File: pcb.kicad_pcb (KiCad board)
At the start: 2 copper layers, 0 parts

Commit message: started layout
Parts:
- added C1: 10uF, Capacitor_SMD:C_0805_2012Metric_Pad1.15x1.40mm_HandSolder, F.Cu at (195.3, 56.5)
- added C2: 10uF, Capacitor_SMD:C_0805_2012Metric_Pad1.15x1.40mm_HandSolder, F.Cu at (195.5, 64.0)
- added C3: 4.7uF, Capacitor_SMD:C_0603_1608Metric_Pad1.05x0.95mm_HandSolder, F.Cu at (195.4, 77.2)
- added C4: 100nF, Capacitor_SMD:C_0603_1608Metric_Pad1.05x0.95mm_HandSolder, F.Cu at (195.6, 82.1)
- added C5: 100nF, Capacitor_SMD:C_0603_1608Metric_Pad1.05x0.95mm_HandSolder, F.Cu at (195.5, 72.7)
- added C6: 100nF, Capacitor_SMD:C_0603_1608Metric_Pad1.05x0.95mm_HandSolder, F.Cu at (195.7, 92.0)
- added C7: 100nF, Capacitor_SMD:C_0603_1608Metric_Pad1.05x0.95mm_HandSolder, F.Cu at (195.6, 87.0)
- added C8: 100nF, Capacitor_SMD:C_0603_1608Metric_Pad1.05x0.95mm_HandSolder, F.Cu at (195.5, 68.3)
- added G1: GPS_NEO_6M_module, components_ece445:GPS_NEO_6M_module, F.Cu at (153.3, 70.9)
- added J1: Conn_01x02, Connector_PinHeader_2.54mm:PinHeader_1x02_P2.54mm_Vertical, F.Cu at (172.8, 32.2)
- added J2: Conn_01x03, Connector_PinHeader_2.54mm:PinHeader_1x03_P2.54mm_Vertical, F.Cu at (112.3, 35.5)
- added J3: Conn_01x03, Connector_PinHeader_2.54mm:PinHeader_1x03_P2.54mm_Vertical, F.Cu at (112.6, 51.8)
- added J4: Conn_01x02, Connector_PinHeader_2.54mm:PinHeader_1x02_P2.54mm_Vertical, F.Cu at (108.8, 96.2)
- added J5: Conn_01x02, Connector_PinHeader_2.54mm:PinHeader_1x02_P2.54mm_Vertical, F.Cu at (120.2, 96.2)
- added J6: Conn_02x05_Odd_Even, Connector_PinHeader_2.54mm:PinHeader_2x05_P2.54mm_Vertical, F.Cu at (93.3, 76.2)
- added Q1: 2N3904, Package_TO_SOT_THT:TO-92_Inline, F.Cu at (99.6, 33.9)
- added Q2: 2N3904, Package_TO_SOT_THT:TO-92_Inline, F.Cu at (99.5, 51.4)
- added Q3: 2N3904, Package_TO_SOT_THT:TO-92_Inline, F.Cu at (99.5, 42.6)
- added Q4: 2N3904, Package_TO_SOT_THT:TO-92_Inline, F.Cu at (99.5, 61.3)
- added R1: 4.7K, Resistor_SMD:R_1206_3216Metric_Pad1.42x1.75mm_HandSolder, F.Cu at (89.0, 36.0)
- added R2: 4.7K, Resistor_SMD:R_1206_3216Metric_Pad1.42x1.75mm_HandSolder, F.Cu at (89.2, 41.1)
- added R3: 1K, Resistor_SMD:R_1206_3216Metric_Pad1.42x1.75mm_HandSolder, F.Cu at (89.1, 46.2)
- added R4: 4.7K, Resistor_SMD:R_1206_3216Metric_Pad1.42x1.75mm_HandSolder, F.Cu at (89.1, 51.2)
- added R5: 4.7K, Resistor_SMD:R_1206_3216Metric_Pad1.42x1.75mm_HandSolder, F.Cu at (89.1, 56.5)
- added R6: 1K, Resistor_SMD:R_1206_3216Metric_Pad1.42x1.75mm_HandSolder, F.Cu at (89.1, 61.7)
- added U1: STM32F103C8T6, STM32F103C8T6:QFP50P900X900X160-48N, F.Cu at (121.0, 81.8)
- added U2: Shaft_encoder, components_ece445:shaft_encoder, F.Cu at (158.7, 36.0)
- added U3: compass_accelerometer, components_ece445:compass_accelerometer, F.Cu at (129.7, 60.1)
- added U4: LM1117-3.3, LM1117DT-3_1:TO228P970X238-3N, F.Cu at (195.2, 43.5)
- added U5: 3v7_to_5V_boost, components_ece445:3v7_to_5V_boost, F.Cu at (175.6, 46.5)

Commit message: evan recommmendations
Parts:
- 3V3 LinReg: renamed from U4
- 5V Boost: renamed from U5
- ARM Conn: renamed from J6
- LI-PO BAT: renamed from J1
- Shaft Encoder: renamed from U2
- moved G1 85.2 mm to (91.4, 129.5)
- moved LI-PO BAT 32.3 mm to (160.8, 62.2)
- moved 3V3 LinReg 31.4 mm to (179.2, 70.5)
- moved C2 31.4 mm to (179.5, 91.0)
- moved C3 31.4 mm to (179.4, 104.2)
- moved C4 31.4 mm to (179.6, 109.1)
- moved C5 31.4 mm to (179.5, 99.7)
- moved C6 31.4 mm to (179.7, 119.0)
- moved C7 31.4 mm to (179.6, 114.0)
- moved C8 31.4 mm to (179.5, 95.3)
- moved C1 31.4 mm to (179.3, 83.5)
- moved R4 31.3 mm to (93.0, 82.3), turned to 180 degrees
- moved Shaft Encoder 31.1 mm to (147.5, 65.0)
- moved J3 31.0 mm to (111.6, 82.8)
- moved Q3 31.0 mm to (98.5, 73.7)
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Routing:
- net +3V3: track 0.00 -> 254.1 mm, vias 0 -> 7
- net +5V: track 0.00 -> 202.1 mm
- net PB14: track 0.00 -> 158.4 mm, vias 0 -> 2
- net PB13: track 0.00 -> 67.2 mm, vias 0 -> 2
- net PB3: track 0.00 -> 60.4 mm
- net GND: track 0.00 -> 56.7 mm, vias 0 -> 56
- net PA13: track 0.00 -> 41.1 mm, vias 0 -> 2
- net PA10: track 0.00 -> 36.8 mm
- net PA9: track 0.00 -> 32.7 mm
- net PA14: track 0.00 -> 30.7 mm, vias 0 -> 2
- net Net-(J2-Pad2): track 0.00 -> 28.6 mm
- net Net-(Q1-Pad3): track 0.00 -> 24.2 mm
- net NRST: track 0.00 -> 22.7 mm
- net PB7: track 0.00 -> 20.3 mm, vias 0 -> 2
- net Net-(Q1-Pad2): track 0.00 -> 20.3 mm
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- added copper zone on F.Cu, net +3V3
- added copper zone on B.Cu, net GND
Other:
- board text added: "+"
- board text added: "-"
- board text added: "3V3"
- board text added: "3V7"
- board text added: "5V"
- board text added: "GND"
- board text added: "RX"
- board text added: "TEAM 2 PCB V1.0 3/2/2022"
- board text added: "TX"

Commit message: made changes into pcb, added python code
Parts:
- removed 3V3 LinReg: LM1117-3.3, LM1117DT-3_1:TO228P970X238-3N
- removed 5V Boost: 3v7_to_5V_boost, components_ece445:3v7_to_5V_boost
- removed ARM Conn: Conn_02x05_Odd_Even, Connector_PinHeader_2.54mm:PinHeader_2x05_P2.54mm_Vertical
- removed J5: Conn_01x02, Connector_PinHeader_2.54mm:PinHeader_1x02_P2.54mm_Vertical
- removed LI-PO BAT: Conn_01x02, Connector_PinHeader_2.54mm:PinHeader_1x02_P2.54mm_Vertical
- removed Shaft Encoder: Shaft_encoder, components_ece445:shaft_encoder
- added C9: 100nF, Capacitor_SMD:C_0603_1608Metric_Pad1.05x0.95mm_HandSolder, F.Cu at (123.4, 128.8)
- added J1: Conn_01x02, Connector_PinHeader_2.54mm:PinHeader_1x02_P2.54mm_Vertical, F.Cu at (89.4, 94.5)
- added J10: Conn_01x03-Connector_Generic, Connector_PinSocket_2.54mm:PinSocket_1x03_P2.54mm_Vertical, F.Cu at (115.8, 120.1)
- added J11: Conn_01x03-Connector_Generic, Connector_PinSocket_2.54mm:PinSocket_1x03_P2.54mm_Vertical, F.Cu at (123.2, 112.0)
- added J6: Conn_01x03-Connector_Generic, Connector_PinSocket_2.54mm:PinSocket_1x03_P2.54mm_Vertical, F.Cu at (79.0, 117.9)
- added J7: Conn_01x03-Connector_Generic, Connector_PinSocket_2.54mm:PinSocket_1x03_P2.54mm_Vertical, F.Cu at (119.6, 93.7)
- added J8: Conn_01x03-Connector_Generic, Connector_PinSocket_2.54mm:PinSocket_1x03_P2.54mm_Vertical, F.Cu at (119.6, 102.9)
- added J9: Conn_01x03-Connector_Generic, Connector_PinSocket_2.54mm:PinSocket_1x03_P2.54mm_Vertical, F.Cu at (115.8, 111.3)
- added R7: 10K, Resistor_SMD:R_1206_3216Metric_Pad1.42x1.75mm_HandSolder, F.Cu at (118.6, 128.8)
- added SW1: SW_Push, Button_Switch_SMD:SW_SPST_PTS645, F.Cu at (120.9, 134.6)
- added U2: Shaft_encoder, components_ece445:shaft_encoder, F.Cu at (99.3, 127.3)
- added U4: LM1117-3.3, LM1117DT-3_1:TO228P970X238-3N, F.Cu at (109.2, 102.8)
- added U5: 3v7_to_5V_boost, components_ece445:3v7_to_5V_boost, F.Cu at (106.2, 91.4)
- J4: value Conn_01x02 -> Conn_01x06; footprint Connector_PinHeader_2.54mm:PinHeader_1x02_P2.54mm_Vertical -> Connector_PinHeader_1.27mm:PinHeader_1x06_P1.27mm_Vertical
- moved C8 79.4 mm to (105.7, 124.5), turned to 0 degrees
- moved C5 76.4 mm to (105.7, 119.1), turned to 0 degrees
- moved C1 75.6 mm to (109.2, 111.8)
- moved C3 74.7 mm to (105.7, 115.6), turned to 0 degrees
- moved C7 74.4 mm to (105.7, 122.7), turned to 0 degrees
- moved C4 74.4 mm to (105.7, 117.3), turned to 0 degrees
- moved C6 74.0 mm to (105.7, 120.9), turned to 0 degrees
- moved C2 72.5 mm to (107.2, 95.5)
- moved U3 48.3 mm to (103.1, 132.1), turned to 0 degrees
- moved J2 45.0 mm to (79.0, 97.8)
- moved J3 40.4 mm to (79.0, 106.7)
- moved Q1 32.7 mm to (97.5, 97.5)
- moved R1 32.2 mm to (90.4, 99.1), turned to 180 degrees
- moved U1 31.7 mm to (89.2, 120.1)
- moved R2 29.6 mm to (90.4, 101.6), turned to 180 degrees
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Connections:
- J4 pad 1: PA0 -> +5V
- J4 pad 2: GND -> RX
- U1 pad 12: Net-(U1-Pad12) -> PA2
- U1 pad 13: Net-(U1-Pad13) -> PA3
- U1 pad 16: Net-(U1-Pad16) -> PA6
- U1 pad 21: Net-(U1-Pad21) -> RX
- U1 pad 22: Net-(U1-Pad22) -> TX
- U1 pad 39: PB3 -> Net-(U1-Pad39)
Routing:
- net +3V3: track 254.1 -> 69.9 mm, vias 7 -> 3
- net PB14: track 158.4 -> 0.00 mm, vias 2 -> 0
- net PB13: track 67.2 -> 0.00 mm, vias 2 -> 0
- net PB3: track 60.4 -> 0.00 mm
- net +5V: track 202.1 -> 154.6 mm
- net GND: track 56.7 -> 15.6 mm, vias 56 -> 3
- net PA10: track 36.8 -> 0.00 mm
- net PA9: track 32.7 -> 0.00 mm
- net Net-(J3-Pad2): track 0.00 -> 27.6 mm
- net PA13: track 41.1 -> 14.6 mm
- net PB7: track 20.3 -> 0.00 mm, vias 2 -> 0
- net Net-(Q2-Pad3): track 0.00 -> 18.7 mm, vias 0 -> 2
- net PB6: track 18.2 -> 0.00 mm
- net PA0: track 18.0 -> 0.00 mm
- net PA1: track 17.3 -> 0.00 mm
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- added copper zone on B.Cu, net +3V3
- added copper zone on F.Cu, net GND
- removed copper zone on F.Cu, net +3V3
- removed copper zone on B.Cu, net GND
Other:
- board text removed: "+"
- board text removed: "-"
- board text removed: "3V3"
- board text removed: "3V7"
- board text removed: "5V"
- board text removed: "GND"
- board text removed: "RX"
- board text removed: "TEAM 2 PCB V1.0 3/2/2022"
- board text removed: "TX"

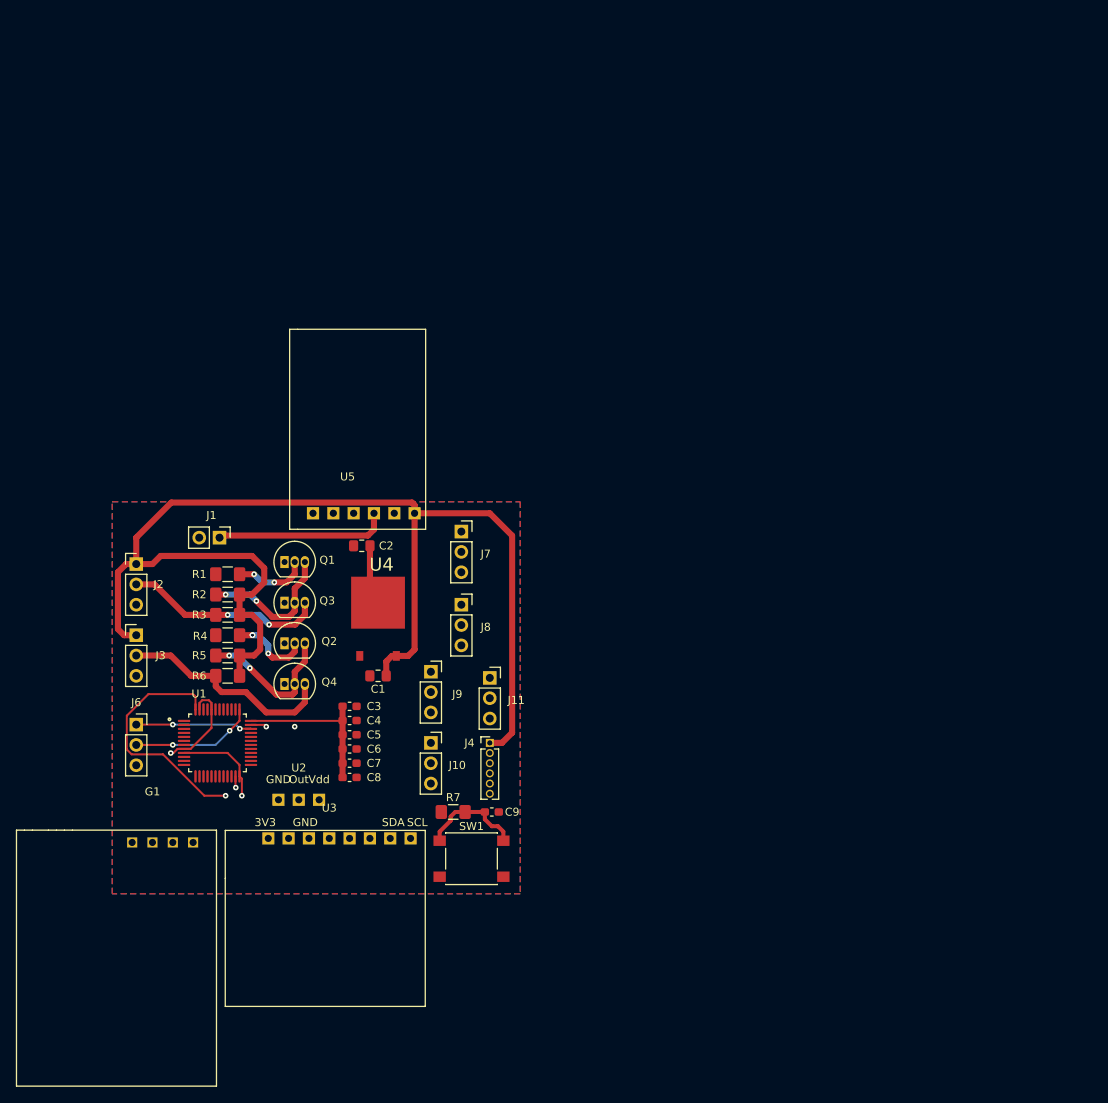
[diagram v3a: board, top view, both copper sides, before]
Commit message: added mounting holes
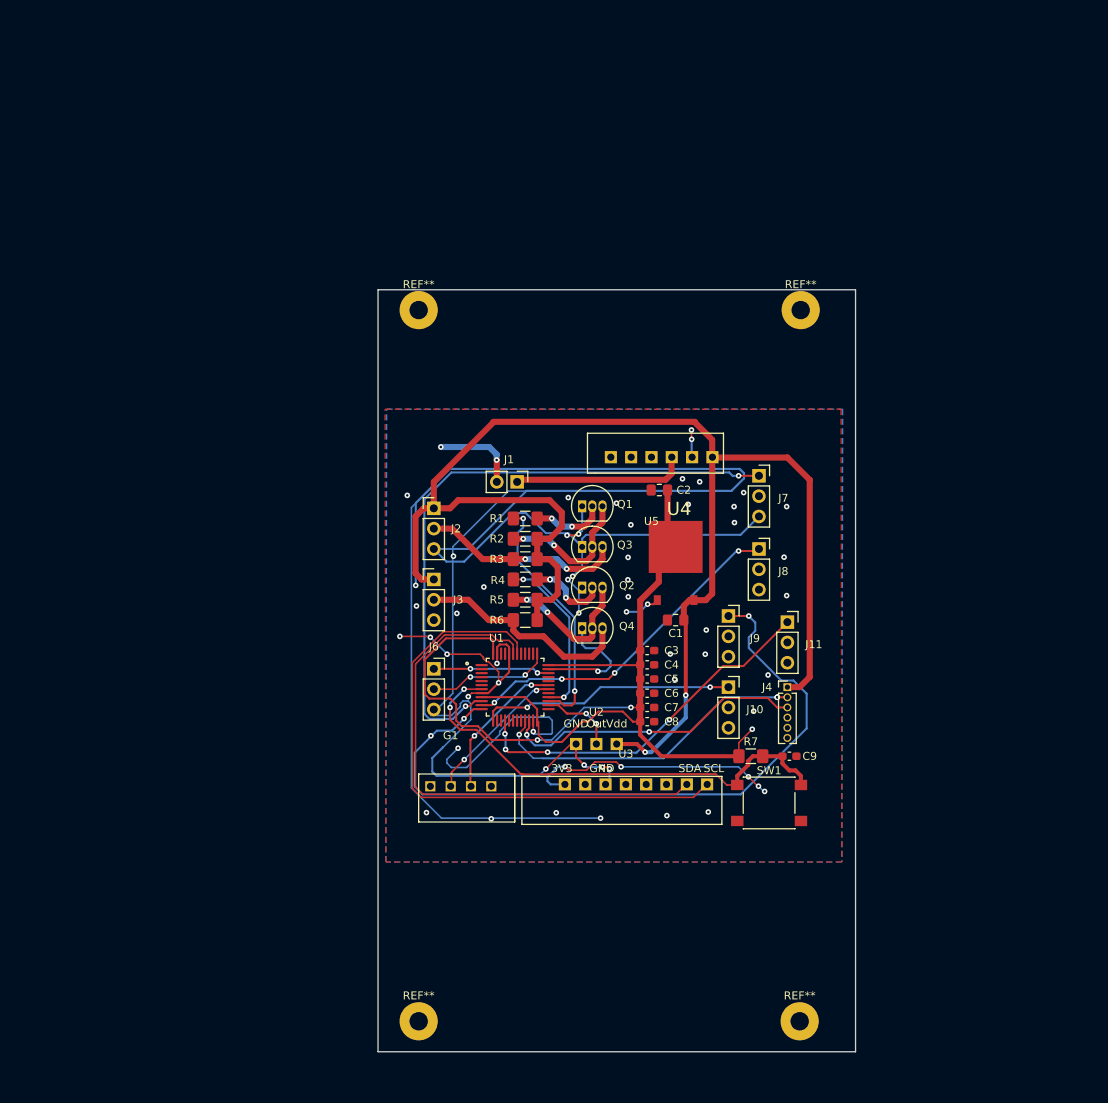
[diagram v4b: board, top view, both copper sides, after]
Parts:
- added REF**: MountingHole_2.2mm_M2, MountingHole:MountingHole_2.2mm_M2, F.Cu at (161.9, 154.9)
- added REF**: MountingHole_2.2mm_M2, MountingHole:MountingHole_2.2mm_M2, F.Cu at (114.3, 154.9)
- added REF**: MountingHole_2.2mm_M2, MountingHole:MountingHole_2.2mm_M2, F.Cu at (162.1, 66.0)
- added REF**: MountingHole_2.2mm_M2, MountingHole:MountingHole_2.2mm_M2, F.Cu at (114.3, 66.0)
- moved G1 37.9 mm to (118.3, 123.0)
- moved U5 37.9 mm to (143.4, 84.4)
- moved R7 37.8 mm to (155.8, 121.8)
- moved SW1 37.8 mm to (158.1, 127.7)
- moved U2 37.8 mm to (136.5, 120.3)
- moved J2 37.8 mm to (116.2, 90.8)
- moved J3 37.8 mm to (116.2, 99.7)
- moved C2 37.8 mm to (144.4, 88.5)
- moved C3 37.8 mm to (142.9, 108.6)
- moved C4 37.8 mm to (142.9, 110.4)
- moved C5 37.8 mm to (142.9, 112.2)
- moved C6 37.8 mm to (142.9, 113.9)
- moved C7 37.8 mm to (142.9, 115.7)
- moved C8 37.8 mm to (142.9, 117.5)
- moved C9 37.8 mm to (160.6, 121.8)
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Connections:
- J10 pad 2: Net-(J10-Pad2) -> (no net)
- J11 pad 2: Net-(J11-Pad2) -> (no net)
- J4 pad 4: Net-(J4-Pad4) -> (no net)
- J4 pad 5: Net-(J4-Pad5) -> (no net)
- J7 pad 2: Net-(J7-Pad2) -> (no net)
- J8 pad 2: Net-(J8-Pad2) -> (no net)
- J9 pad 2: Net-(J9-Pad2) -> (no net)
- U1 pad 1: Net-(U1-Pad1) -> (no net)
- U1 pad 14: Net-(U1-Pad14) -> (no net)
- U1 pad 15: Net-(U1-Pad15) -> (no net)
- U1 pad 17: Net-(U1-Pad17) -> (no net)
- U1 pad 18: Net-(U1-Pad18) -> (no net)
- U1 pad 19: Net-(U1-Pad19) -> (no net)
- U1 pad 2: Net-(U1-Pad2) -> (no net)
- U1 pad 20: Net-(U1-Pad20) -> (no net)
- U1 pad 25: Net-(U1-Pad25) -> (no net)
- U1 pad 29: Net-(U1-Pad29) -> (no net)
- U1 pad 3: Net-(U1-Pad3) -> (no net)
- U1 pad 32: Net-(U1-Pad32) -> (no net)
- U1 pad 33: Net-(U1-Pad33) -> (no net)
- U1 pad 38: Net-(U1-Pad38) -> (no net)
- U1 pad 39: Net-(U1-Pad39) -> (no net)
- U1 pad 4: Net-(U1-Pad4) -> (no net)
- U1 pad 40: Net-(U1-Pad40) -> (no net)
- U1 pad 41: Net-(U1-Pad41) -> (no net)
- U1 pad 45: Net-(U1-Pad45) -> (no net)
- U1 pad 46: Net-(U1-Pad46) -> (no net)
- U1 pad 5: Net-(U1-Pad5) -> (no net)
- U1 pad 6: Net-(U1-Pad6) -> (no net)
- U3 pad 4: Net-(U3-Pad4) -> (no net)
- U3 pad 5: Net-(U3-Pad5) -> (no net)
- U3 pad 6: Net-(U3-Pad6) -> (no net)
- U3 pad 8: Net-(U3-Pad8) -> (no net)
- U5 pad 1: Net-(U5-Pad1) -> (no net)
- U5 pad 2: Net-(U5-Pad2) -> (no net)
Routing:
- net GND: track 15.6 -> 459.0 mm, vias 3 -> 57
- net +3V3: track 69.9 -> 168.6 mm, vias 3 -> 8
- net PA2: track 0.00 -> 88.8 mm, vias 0 -> 3
- net PA0: track 0.00 -> 78.5 mm, vias 0 -> 2
- net PB6: track 0.00 -> 70.6 mm
- net PB7: track 0.00 -> 65.7 mm
- net NRST: track 13.1 -> 59.1 mm, vias 0 -> 2
- net PA6: track 0.00 -> 45.8 mm, vias 0 -> 4
- net PA1: track 0.00 -> 42.7 mm, vias 0 -> 4
- net RX: track 0.00 -> 40.7 mm, vias 0 -> 3
- net TX: track 0.00 -> 38.1 mm, vias 0 -> 2
- net PA3: track 0.00 -> 31.8 mm, vias 0 -> 2
- net PB14: track 0.00 -> 31.1 mm, vias 0 -> 2
- net +5V: track 154.6 -> 181.0 mm, vias 0 -> 2
- net PB15: track 0.00 -> 21.1 mm, vias 0 -> 2
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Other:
- board outline added: 59.7 x 95.2 mm

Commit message: final changes to PCB
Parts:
- J4: footprint Connector_PinHeader_1.27mm:PinHeader_1x06_P1.27mm_Vertical -> Connector_Hirose:Hirose_DF13-06P-1.25DSA_1x06_P1.25mm_Vertical
- R1, R2, R3, R4, R5, R6, R7: footprint Resistor_SMD:R_1206_3216Metric_Pad1.42x1.75mm_HandSolder -> Resistor_SMD:R_0805_2012Metric_Pad1.15x1.40mm_HandSolder
- moved J3 47.5 mm to (162.6, 110.2)
- moved J2 47.5 mm to (162.6, 101.0)
- moved J11 44.2 mm to (117.7, 116.8), turned to 270 degrees
- moved J7 44.1 mm to (113.4, 94.7)
- moved J10 40.0 mm to (113.0, 112.6), turned to 180 degrees
- moved J8 40.0 mm to (117.6, 103.7), turned to 180 degrees
- moved J9 36.5 mm to (117.6, 113.0), turned to 180 degrees
- moved R1 36.3 mm to (155.8, 115.0), turned to 0 degrees
- moved J1 33.6 mm to (159.5, 94.5), turned to 90 degrees
- moved R2 33.4 mm to (155.8, 112.6), turned to 0 degrees
- moved J4 32.0 mm to (128.8, 117.9), turned to 180 degrees
- moved R3 31.0 mm to (155.8, 110.0), turned to 0 degrees
- moved Q1 29.9 mm to (151.1, 115.6), turned to 180 degrees
- moved R4 29.3 mm to (155.8, 107.5), turned to 0 degrees
- moved R5 28.3 mm to (155.8, 105.0), turned to 0 degrees
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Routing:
- net GND: track 459.0 -> 24.6 mm, vias 57 -> 5
- net PA2: track 88.8 -> 5.19 mm, vias 3 -> 0
- net PA0: track 78.5 -> 22.8 mm, vias 2 -> 0
- net PA9: track 18.6 -> 57.9 mm
- net RX: track 40.7 -> 4.27 mm, vias 3 -> 0
- net PA6: track 45.8 -> 9.94 mm, vias 4 -> 0
- net PB6: track 70.6 -> 37.6 mm, vias 0 -> 3
- net PA1: track 42.7 -> 11.9 mm, vias 4 -> 0
- net PA10: track 18.5 -> 48.1 mm
- net +3V3: track 168.6 -> 139.9 mm, vias 8 -> 6
- net TX: track 38.1 -> 10.0 mm, vias 2 -> 0
- net NRST: track 59.1 -> 86.5 mm, vias 2 -> 4
- net +5V: track 181.0 -> 153.8 mm, vias 2 -> 8
- net PA3: track 31.8 -> 13.7 mm, vias 2 -> 0
- net PB7: track 65.7 -> 48.4 mm, vias 0 -> 2
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- added copper zone on B.Cu, net GND
- removed copper zone on B.Cu, net +3V3

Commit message: second round pcb
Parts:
- added J12: USB_B_Micro, Connector_USB:USB_Micro-B_Molex-105133-0031, F.Cu at (132.5, 84.8)
- added J5: Conn_02x03, Connector_PinHeader_2.54mm:PinHeader_2x03_P2.54mm_Vertical, F.Cu at (142.4, 100.7)
- added R10: 20R, Resistor_SMD:R_0805_2012Metric_Pad1.15x1.40mm_HandSolder, F.Cu at (159.8, 87.2)
- added R11: 20R, Resistor_SMD:R_0805_2012Metric_Pad1.15x1.40mm_HandSolder, F.Cu at (159.8, 89.4)
- added R12: 4.7K, Resistor_SMD:R_0805_2012Metric_Pad1.15x1.40mm_HandSolder, F.Cu at (159.8, 85.1)
- added R8: 100K, Resistor_SMD:R_0805_2012Metric_Pad1.15x1.40mm_HandSolder, F.Cu at (134.4, 89.9)
- added R9: 100K, Resistor_SMD:R_0805_2012Metric_Pad1.15x1.40mm_HandSolder, F.Cu at (145.8, 112.6)
- J6: footprint Connector_PinSocket_2.54mm:PinSocket_1x03_P2.54mm_Vertical -> Connector_PinHeader_2.54mm:PinHeader_1x03_P2.54mm_Horizontal
- moved J6 7.05 mm to (118.6, 94.0), turned to 90 degrees
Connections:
- U1 pad 20: (no net) -> BOOT1
- U1 pad 32: (no net) -> PA11
- U1 pad 33: (no net) -> PA12
- U1 pad 44: GND -> BOOT0
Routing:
- net BOOT1: track 0.00 -> 78.5 mm, vias 0 -> 4
- net +5V: track 153.8 -> 213.0 mm, vias 8 -> 10
- net PA12: track 0.00 -> 57.9 mm, vias 0 -> 4
- net Net-(J12-Pad2): track 0.00 -> 43.1 mm, vias 0 -> 2
- net PA11: track 0.00 -> 39.9 mm, vias 0 -> 4
- net Net-(J12-Pad3): track 0.00 -> 38.7 mm, vias 0 -> 2
- net BOOT0: track 0.00 -> 23.3 mm, vias 0 -> 2
- net Net-(J5-Pad3): track 0.00 -> 17.9 mm, vias 0 -> 1
- net +3V3: track 139.9 -> 153.7 mm
- net Net-(J5-Pad4): track 0.00 -> 9.07 mm, vias 0 -> 1
- net PA13: track 14.1 -> 21.7 mm
- net GND: track 24.6 -> 31.9 mm, vias 5 -> 64
- net PA14: track 12.2 -> 16.0 mm
